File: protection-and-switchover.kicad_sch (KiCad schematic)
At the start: 18 parts, among them Q1 Q_NMOS_DGS, U5 TPS2662x, U6 TPS2662x

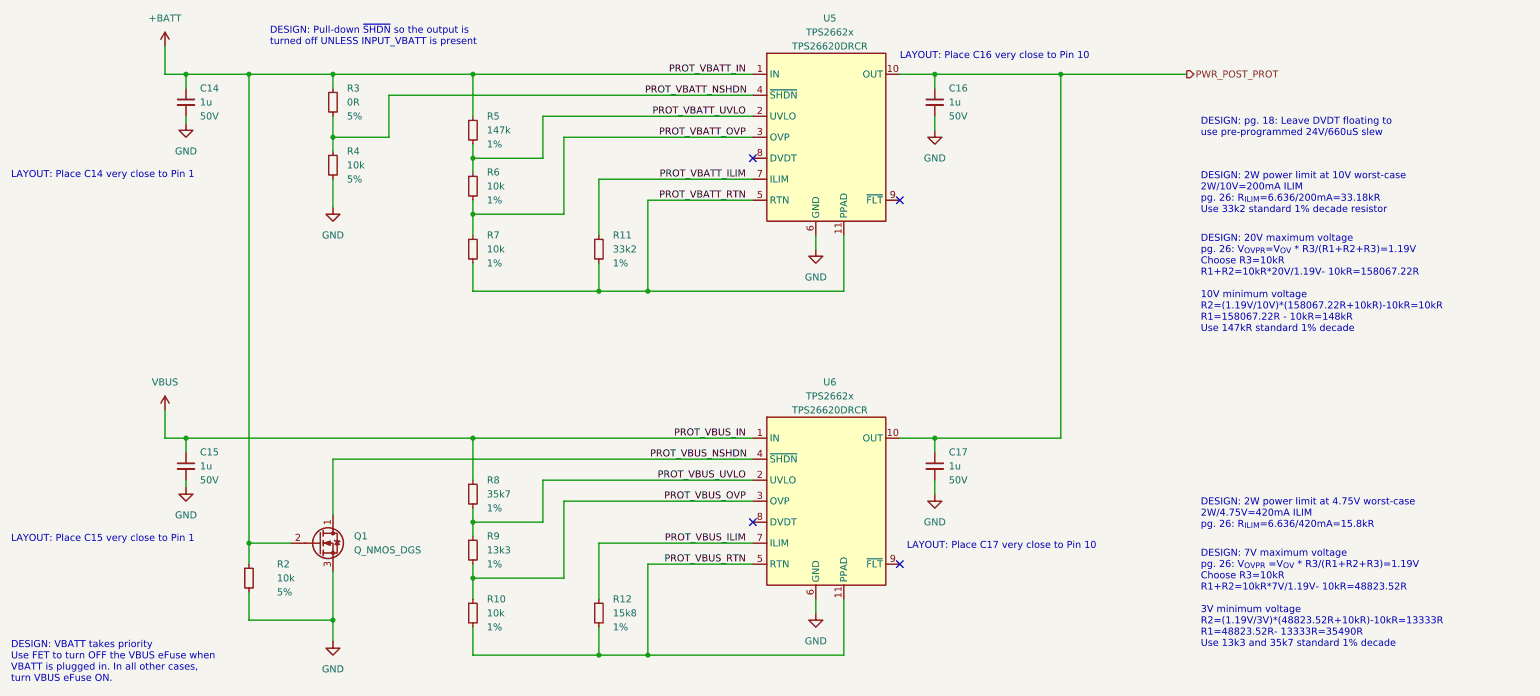
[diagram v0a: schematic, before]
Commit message: Update tolerances, finish BOM
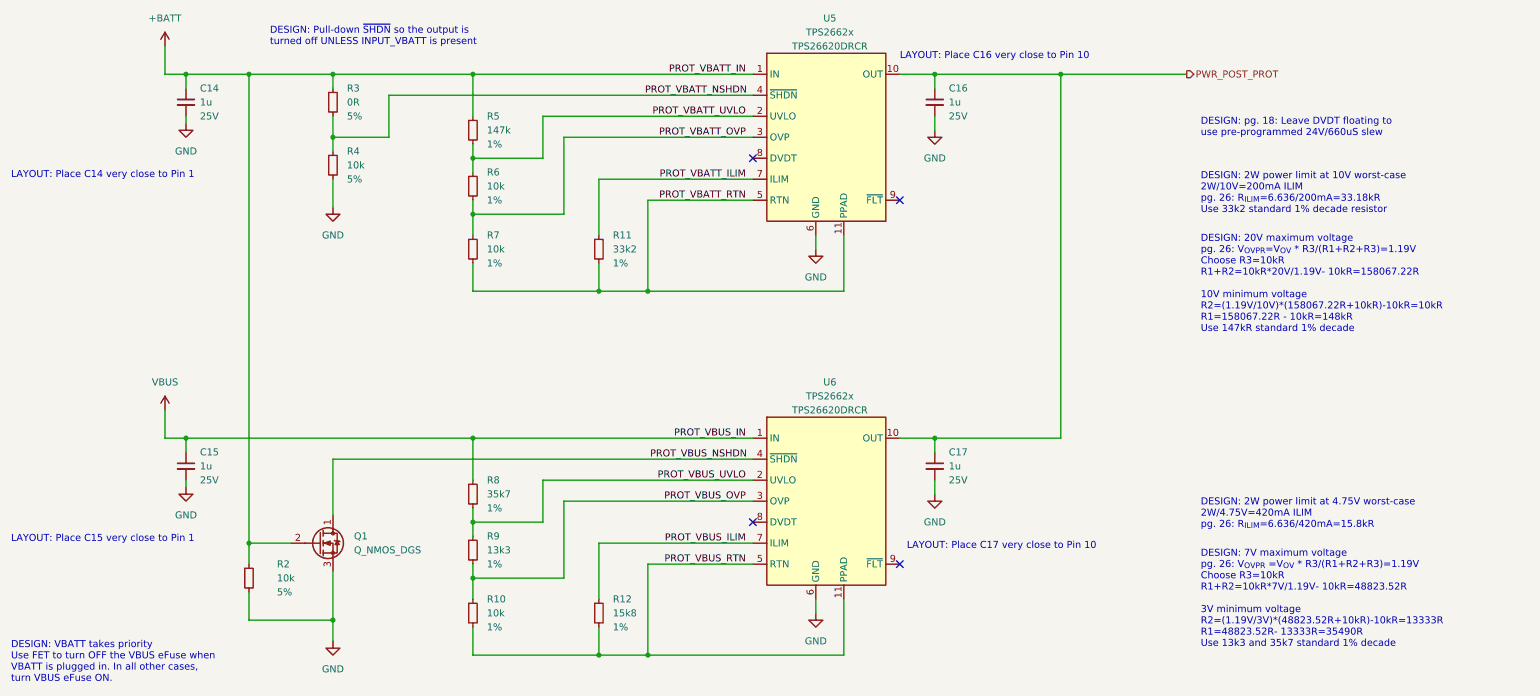
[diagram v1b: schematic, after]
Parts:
- C14, C15, C16, C17: Rating 50V -> 25V
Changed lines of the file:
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@@
       (effects (font (size 1.27 1.27)) hide)
     )
-    (property "Rating" "50V" (id 4) (at 50.8 50.7938 0)
+    (property "Rating" "25V" (id 4) (at 50.8 50.7938 0)
       (effects (font (size 1.27 1.27)) (justify left))
     )
@@
       (effects (font (size 1.27 1.27)) hide)
     )
-    (property "Rating" "50V" (id 4) (at 186.69 50.7938 0)
+    (property "Rating" "25V" (id 4) (at 186.69 50.7938 0)
       (effects (font (size 1.27 1.27)) (justify left))
     )
@@
       (effects (font (size 1.27 1.27)) hide)
     )
-    (property "Rating" "50V" (id 4) (at 50.8 116.8338 0)
+    (property "Rating" "25V" (id 4) (at 50.8 116.8338 0)
       (effects (font (size 1.27 1.27)) (justify left))
     )
@@
       (effects (font (size 1.27 1.27)) hide)
     )
-    (property "Rating" "50V" (id 4) (at 186.69 116.8338 0)
+    (property "Rating" "25V" (id 4) (at 186.69 116.8338 0)
       (effects (font (size 1.27 1.27)) (justify left))
     )

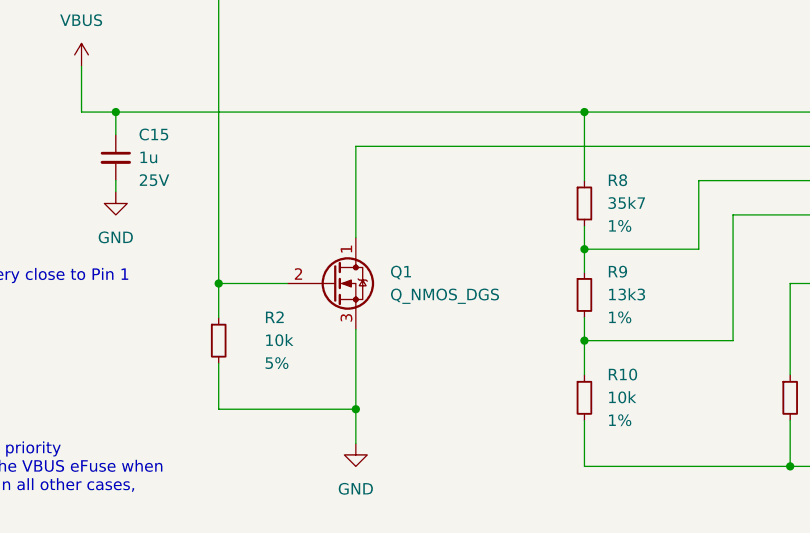
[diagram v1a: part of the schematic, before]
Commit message: Correct error with FET pinout
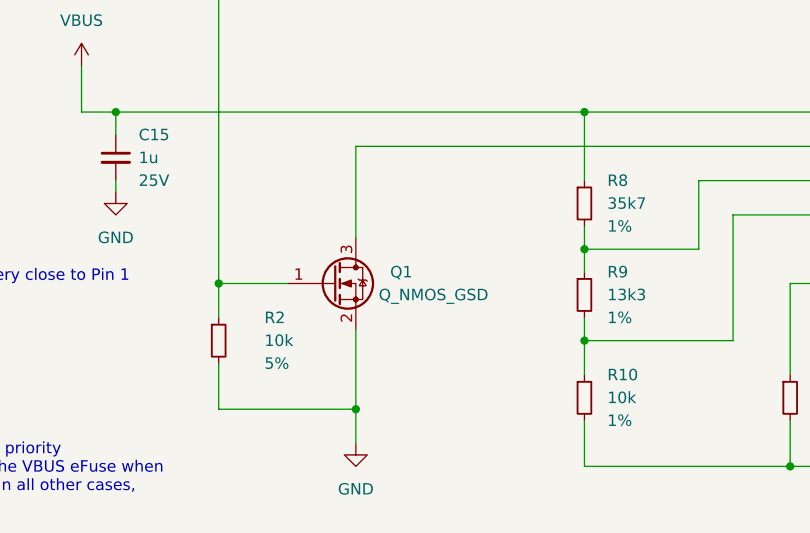
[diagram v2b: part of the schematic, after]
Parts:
- Q1: value Q_NMOS_DGS -> Q_NMOS_GSD; symbol Device:Q_NMOS_DGS -> Device:Q_NMOS_GSD
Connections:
- net +BATT: now also Q1.1 (G); no longer Q1.2 (G)
- net GND: now also Q1.2 (S); no longer Q1.3 (S)
- net PROT_VBUS_NSHDN: now also Q1.3 (D); no longer Q1.1 (D)
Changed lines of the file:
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@@
     (pin "1")
   )
-  (symbol (lib_id "Device:Q_NMOS_DGS") (at 72.39 128.27 0) (unit 1)
+  (symbol (lib_id "Device:Q_NMOS_GSD") (at 72.39 128.27 0) (unit 1)
     (in_bom yes) (on_board yes) (fields_autoplaced)
     (property "Reference" "Q1" (id 0) (at 78.74 126.9999 0)
       (effects (font (size 1.27 1.27)) (justify left))
     )
-    (property "Value" "Q_NMOS_DGS" (id 1) (at 78.74 129.5399 0)
+    (property "Value" "Q_NMOS_GSD" (id 1) (at 77.47 129.54 0)
       (effects (font (size 1.27 1.27)) (justify left))
     )
